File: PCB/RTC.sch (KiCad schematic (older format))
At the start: 5 parts, among them U8 DS3231M

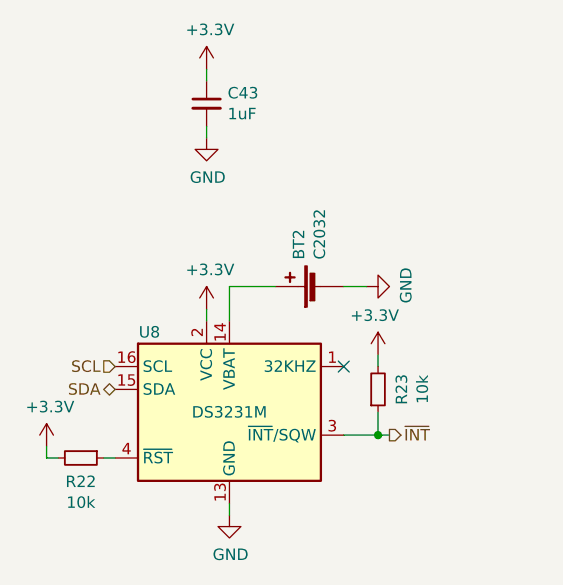
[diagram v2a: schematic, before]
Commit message: Increased VCC from 3v3 to 5v
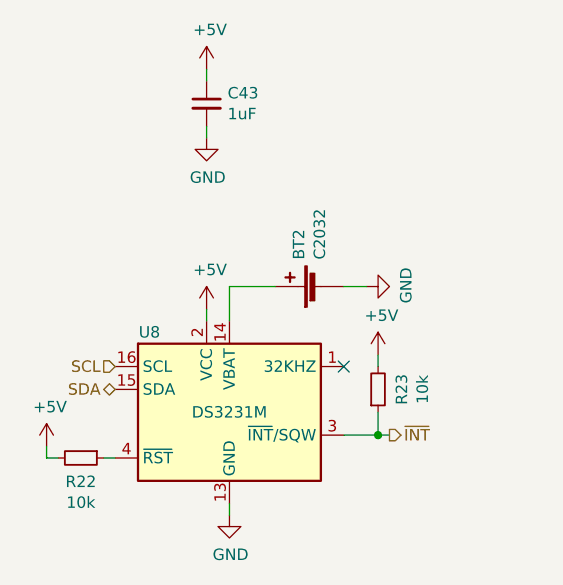
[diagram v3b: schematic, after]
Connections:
- net +3V3 renamed +5V
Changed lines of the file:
@@
 $Descr A4 11693 8268
 encoding utf-8
-Sheet 15 25
+Sheet 16 25
 Title ""
 Date ""
@@
 	0    -1   -1   0
 $EndComp
-$Comp
-L power:+3.3V #PWR0118
-U 1 1 5E875558
-P 5500 3650
-F 0 "#PWR0118" H 5500 3500 50  0001 C CNN
-F 1 "+3.3V" H 5515 3823 50  0000 C CNN
-F 2 "" H 5500 3650 50  0001 C CNN
-F 3 "" H 5500 3650 50  0001 C CNN
-	1    5500 3650
-	1    0    0    -1
-$EndComp
 Wire Wire Line
 	5500 3650 5500 3700
@@
 	1    0    0    -1
 $EndComp
-$Comp
-L power:+3.3V #PWR0116
-U 1 1 5E879CC5
-P 5500 2600
-F 0 "#PWR0116" H 5500 2450 50  0001 C CNN
-F 1 "+3.3V" H 5515 2773 50  0000 C CNN
-F 2 "" H 5500 2600 50  0001 C CNN
-F 3 "" H 5500 2600 50  0001 C CNN
-	1    5500 2600
-	1    0    0    -1
-$EndComp
 Wire Wire Line
 	5500 2600 5500 2650
@@
 	0    1    1    0
 $EndComp
-$Comp
-L power:+3.3V #PWR0115
-U 1 1 5E87C09D
-P 4800 4250
-F 0 "#PWR0115" H 4800 4100 50  0001 C CNN
-F 1 "+3.3V" H 4815 4423 50  0000 C CNN
-F 2 "" H 4800 4250 50  0001 C CNN
-F 3 "" H 4800 4250 50  0001 C CNN
-	1    4800 4250
-	1    0    0    -1
-$EndComp
 Wire Wire Line
 	4800 4250 4800 4300
@@
 	1    0    0    1
 $EndComp
-$Comp
-L power:+3.3V #PWR0121
-U 1 1 5E87E247
-P 6250 3850
-F 0 "#PWR0121" H 6250 3700 50  0001 C CNN
-F 1 "+3.3V" H 6265 4023 50  0000 C CNN
-F 2 "" H 6250 3850 50  0001 C CNN
-F 3 "" H 6250 3850 50  0001 C CNN
-	1    6250 3850
-	-1   0    0    -1
-$EndComp
 Wire Wire Line
 	6100 4200 6250 4200
@@
 	6300 4200 6250 4200
 Connection ~ 6250 4200
+$Comp
+L power:+5V #PWR?
+U 1 1 5E91AA2A
+P 4800 4250
+AR Path="/5E8A6686/5E91AA2A" Ref="#PWR?"  Part="1"
+AR Path="/5E87171F/5E91AA2A" Ref="#PWR?"  Part="1"
+F 0 "#PWR?" H 4800 4100 50  0001 C CNN
+F 1 "+5V" H 4815 4423 50  0000 C CNN
+F 2 "" H 4800 4250 50  0001 C CNN
+F 3 "" H 4800 4250 50  0001 C CNN
+	1    4800 4250
+	1    0    0    -1
+$EndComp
+$Comp
+L power:+5V #PWR?
+U 1 1 5E91AB6A
+P 5500 3650
+AR Path="/5E8A6686/5E91AB6A" Ref="#PWR?"  Part="1"
+AR Path="/5E87171F/5E91AB6A" Ref="#PWR?"  Part="1"
+F 0 "#PWR?" H 5500 3500 50  0001 C CNN
+F 1 "+5V" H 5515 3823 50  0000 C CNN
+F 2 "" H 5500 3650 50  0001 C CNN
+F 3 "" H 5500 3650 50  0001 C CNN
+	1    5500 3650
+	1    0    0    -1
+$EndComp
+$Comp
+L power:+5V #PWR?
+U 1 1 5E91B25B
+P 5500 2600
+F 0 "#PWR?" H 5500 2450 50  0001 C CNN
+F 1 "+5V" H 5515 2773 50  0000 C CNN
+F 2 "" H 5500 2600 50  0001 C CNN
+F 3 "" H 5500 2600 50  0001 C CNN
+	1    5500 2600
+	1    0    0    -1
+$EndComp
+$Comp
+L power:+5V #PWR?
+U 1 1 5E91BBAD
+P 6250 3850
+F 0 "#PWR?" H 6250 3700 50  0001 C CNN
+F 1 "+5V" H 6265 4023 50  0000 C CNN
+F 2 "" H 6250 3850 50  0001 C CNN
+F 3 "" H 6250 3850 50  0001 C CNN
+	1    6250 3850
+	1    0    0    -1
+$EndComp
 $EndSCHEMATC

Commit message: Added Humidity and temperature sensors
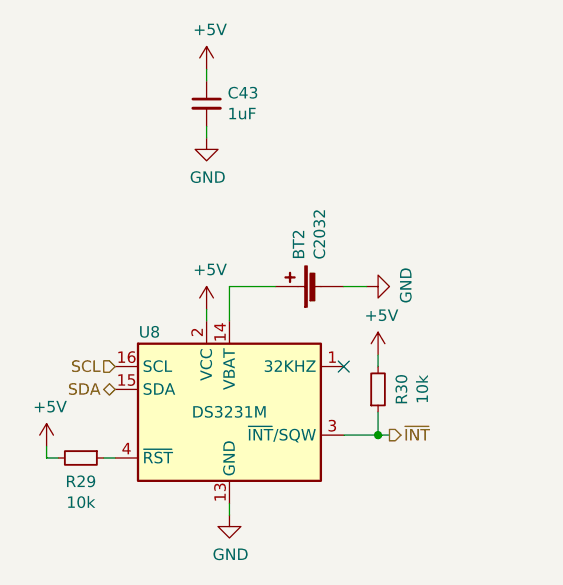
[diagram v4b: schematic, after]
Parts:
- renumbered R22 to R29, R23 to R30
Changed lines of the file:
@@
 $EndComp
 $Comp
-L power:GND #PWR0120
+L power:GND #PWR0123
 U 1 1 5E87532F
 P 6200 3550
-F 0 "#PWR0120" H 6200 3300 50  0001 C CNN
+F 0 "#PWR0123" H 6200 3300 50  0001 C CNN
 F 1 "GND" H 6205 3377 50  0000 C CNN
 F 2 "" H 6200 3550 50  0001 C CNN
@@
 NoConn ~ 6100 3900
 $Comp
-L power:GND #PWR0119
+L power:GND #PWR0122
 U 1 1 5E878241
 P 5600 4550
-F 0 "#PWR0119" H 5600 4300 50  0001 C CNN
+F 0 "#PWR0122" H 5600 4300 50  0001 C CNN
 F 1 "GND" H 5605 4377 50  0000 C CNN
 F 2 "" H 5600 4550 50  0001 C CNN
@@
 	5500 2600 5500 2650
 $Comp
-L power:GND #PWR0117
+L power:GND #PWR0120
 U 1 1 5E87A00D
 P 5500 2900
-F 0 "#PWR0117" H 5500 2650 50  0001 C CNN
+F 0 "#PWR0120" H 5500 2650 50  0001 C CNN
 F 1 "GND" H 5505 2727 50  0000 C CNN
 F 2 "" H 5500 2900 50  0001 C CNN
@@
 	5500 2850 5500 2900
 $Comp
-L Device:R_Small R22
+L Device:R_Small R29
 U 1 1 5E87BE49
 P 4950 4300
-F 0 "R22" V 5054 4300 50  0000 C CNN
+F 0 "R29" V 5054 4300 50  0000 C CNN
 F 1 "10k" V 5145 4300 50  0000 C CNN
 F 2 "" H 4950 4300 50  0001 C CNN
@@
 	5050 4300 5100 4300
 $Comp
-L Device:R_Small R23
+L Device:R_Small R30
 U 1 1 5E87E241
 P 6250 4000
-F 0 "R23" V 6354 4000 50  0000 C CNN
+F 0 "R30" V 6354 4000 50  0000 C CNN
 F 1 "10k" V 6445 4000 50  0000 C CNN
 F 2 "" H 6250 4000 50  0001 C CNN
@@
 P 4800 4250
 AR Path="/5E8A6686/5E91AA2A" Ref="#PWR?"  Part="1"
-AR Path="/5E87171F/5E91AA2A" Ref="#PWR?"  Part="1"
-F 0 "#PWR?" H 4800 4100 50  0001 C CNN
+AR Path="/5E87171F/5E91AA2A" Ref="#PWR0118"  Part="1"
+F 0 "#PWR0118" H 4800 4100 50  0001 C CNN
 F 1 "+5V" H 4815 4423 50  0000 C CNN
 F 2 "" H 4800 4250 50  0001 C CNN
@@
 P 5500 3650
 AR Path="/5E8A6686/5E91AB6A" Ref="#PWR?"  Part="1"
-AR Path="/5E87171F/5E91AB6A" Ref="#PWR?"  Part="1"
-F 0 "#PWR?" H 5500 3500 50  0001 C CNN
+AR Path="/5E87171F/5E91AB6A" Ref="#PWR0121"  Part="1"
+F 0 "#PWR0121" H 5500 3500 50  0001 C CNN
 F 1 "+5V" H 5515 3823 50  0000 C CNN
 F 2 "" H 5500 3650 50  0001 C CNN
@@
 U 1 1 5E91B25B
 P 5500 2600
-F 0 "#PWR?" H 5500 2450 50  0001 C CNN
+AR Path="/5E8A6686/5E91B25B" Ref="#PWR?"  Part="1"
+AR Path="/5E87171F/5E91B25B" Ref="#PWR0119"  Part="1"
+F 0 "#PWR0119" H 5500 2450 50  0001 C CNN
 F 1 "+5V" H 5515 2773 50  0000 C CNN
 F 2 "" H 5500 2600 50  0001 C CNN
@@
 U 1 1 5E91BBAD
 P 6250 3850
-F 0 "#PWR?" H 6250 3700 50  0001 C CNN
+AR Path="/5E8A6686/5E91BBAD" Ref="#PWR?"  Part="1"
+AR Path="/5E87171F/5E91BBAD" Ref="#PWR0124"  Part="1"
+F 0 "#PWR0124" H 6250 3700 50  0001 C CNN
 F 1 "+5V" H 6265 4023 50  0000 C CNN
 F 2 "" H 6250 3850 50  0001 C CNN

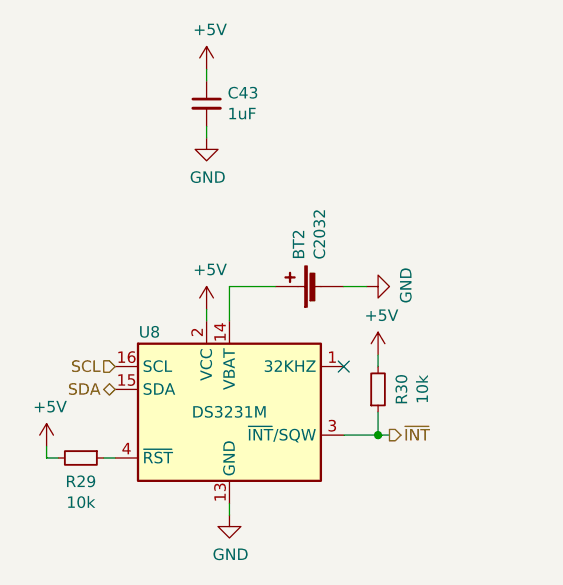
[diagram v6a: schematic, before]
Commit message: Added correct DRV breakout and added testpoints
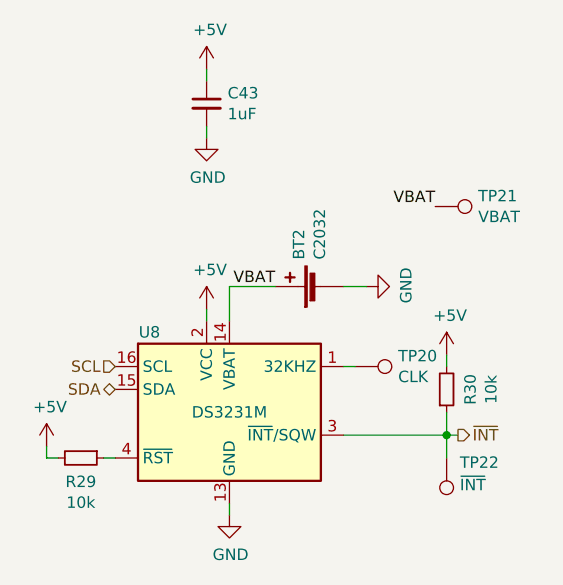
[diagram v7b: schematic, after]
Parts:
- added TP20: CLK, symbol Connector:TestPoint
- added TP21: VBAT, symbol Connector:TestPoint
- added TP22: ~INT, symbol Connector:TestPoint
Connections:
- net ~INT: now also TP22.1
- net at U8.1 (32KHZ): now also TP20.1
- net VBAT: now reaches BT2.1 (+), U8.14 (VBAT)
- net VBAT: now also TP21.1
- no-connect marks 1 -> 0
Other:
- moved on the sheet: R30
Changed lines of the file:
@@
 $EndComp
-Wire Wire Line
-	5500 3650 5500 3700
 Wire Wire Line
 	5800 3550 5600 3550
@@
 Wire Wire Line
 	6100 3550 6200 3550
-NoConn ~ 6100 3900
 $Comp
 L power:GND #PWR0122
@@
 L Device:R_Small R30
 U 1 1 5E87E241
-P 6250 4000
-F 0 "R30" V 6354 4000 50  0000 C CNN
-F 1 "10k" V 6445 4000 50  0000 C CNN
-F 2 "" H 6250 4000 50  0001 C CNN
-F 3 "" H 6250 4000 50  0001 C CNN
-	1    6250 4000
+P 6550 4000
+F 0 "R30" V 6654 4000 50  0000 C CNN
+F 1 "10k" V 6745 4000 50  0000 C CNN
+F 2 "" H 6550 4000 50  0001 C CNN
+F 3 "" H 6550 4000 50  0001 C CNN
+	1    6550 4000
 	1    0    0    1
 $EndComp
 Wire Wire Line
-	6100 4200 6250 4200
+	6100 4200 6550 4200
 Wire Wire Line
-	6250 4200 6250 4100
+	6550 4200 6550 4100
 Wire Wire Line
-	6250 3900 6250 3850
-Text HLabel 6300 4200 2    50   Output ~ 0
+	6550 3900 6550 3850
+Text HLabel 6600 4200 2    50   Output ~ 0
 ~INT
 Wire Wire Line
-	6300 4200 6250 4200
-Connection ~ 6250 4200
+	6600 4200 6550 4200
+Connection ~ 6550 4200
 $Comp
 L power:+5V #PWR?
@@
 F 3 "" H 4800 4250 50  0001 C CNN
 	1    4800 4250
-	1    0    0    -1
-$EndComp
-$Comp
-L power:+5V #PWR?
-U 1 1 5E91AB6A
-P 5500 3650
-AR Path="/5E8A6686/5E91AB6A" Ref="#PWR?"  Part="1"
-AR Path="/5E87171F/5E91AB6A" Ref="#PWR0121"  Part="1"
-F 0 "#PWR0121" H 5500 3500 50  0001 C CNN
-F 1 "+5V" H 5515 3823 50  0000 C CNN
-F 2 "" H 5500 3650 50  0001 C CNN
-F 3 "" H 5500 3650 50  0001 C CNN
-	1    5500 3650
 	1    0    0    -1
 $EndComp
@@
 L power:+5V #PWR?
 U 1 1 5E91BBAD
-P 6250 3850
+P 6550 3850
 AR Path="/5E8A6686/5E91BBAD" Ref="#PWR?"  Part="1"
 AR Path="/5E87171F/5E91BBAD" Ref="#PWR0124"  Part="1"
-F 0 "#PWR0124" H 6250 3700 50  0001 C CNN
-F 1 "+5V" H 6265 4023 50  0000 C CNN
-F 2 "" H 6250 3850 50  0001 C CNN
-F 3 "" H 6250 3850 50  0001 C CNN
-	1    6250 3850
+F 0 "#PWR0124" H 6550 3700 50  0001 C CNN
+F 1 "+5V" H 6565 4023 50  0000 C CNN
+F 2 "" H 6550 3850 50  0001 C CNN
+F 3 "" H 6550 3850 50  0001 C CNN
+	1    6550 3850
 	1    0    0    -1
 $EndComp
+$Comp
+L Connector:TestPoint TP?
+U 1 1 5E93A279
+P 6150 3900
+AR Path="/5E93A279" Ref="TP?"  Part="1"
+AR Path="/5E87171F/5E93A279" Ref="TP20"  Part="1"
+F 0 "TP20" V 6104 4088 50  0000 L CNN
+F 1 "CLK" V 6195 4088 50  0000 L CNN
+F 2 "" H 6350 3900 50  0001 C CNN
+F 3 "~" H 6350 3900 50  0001 C CNN
+	1    6150 3900
+	0    1    1    0
+$EndComp
+$Comp
+L Connector:TestPoint TP?
+U 1 1 5E93A65A
+P 6550 4300
+AR Path="/5E93A65A" Ref="TP?"  Part="1"
+AR Path="/5E87171F/5E93A65A" Ref="TP22"  Part="1"
+F 0 "TP22" H 6492 4320 50  0000 R CNN
+F 1 "~INT" H 6492 4418 50  0000 R CNN
+F 2 "" H 6750 4300 50  0001 C CNN
+F 3 "~" H 6750 4300 50  0001 C CNN
+	1    6550 4300
+	-1   0    0    1
+$EndComp
+Wire Wire Line
+	6150 3900 6100 3900
+Wire Wire Line
+	6550 4300 6550 4200
+$Comp
+L Connector:TestPoint TP?
+U 1 1 5E93C9CD
+P 6500 3200
+AR Path="/5E93C9CD" Ref="TP?"  Part="1"
+AR Path="/5E87171F/5E93C9CD" Ref="TP21"  Part="1"
+F 0 "TP21" V 6454 3388 50  0000 L CNN
+F 1 "VBAT" V 6545 3388 50  0000 L CNN
+F 2 "" H 6700 3200 50  0001 C CNN
+F 3 "~" H 6700 3200 50  0001 C CNN
+	1    6500 3200
+	0    1    1    0
+$EndComp
+Wire Wire Line
+	5500 3650 5500 3700
+$Comp
+L power:+5V #PWR?
+U 1 1 5E91AB6A
+P 5500 3650
+AR Path="/5E8A6686/5E91AB6A" Ref="#PWR?"  Part="1"
+AR Path="/5E87171F/5E91AB6A" Ref="#PWR0121"  Part="1"
+F 0 "#PWR0121" H 5500 3500 50  0001 C CNN
+F 1 "+5V" H 5515 3823 50  0000 C CNN
+F 2 "" H 5500 3650 50  0001 C CNN
+F 3 "" H 5500 3650 50  0001 C CNN
+	1    5500 3650
+	1    0    0    -1
+$EndComp
+Text Label 6500 3200 2    50   ~ 0
+VBAT
+Text Label 5800 3550 2    50   ~ 0
+VBAT
 $EndSCHEMATC

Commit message: Added remaining test points
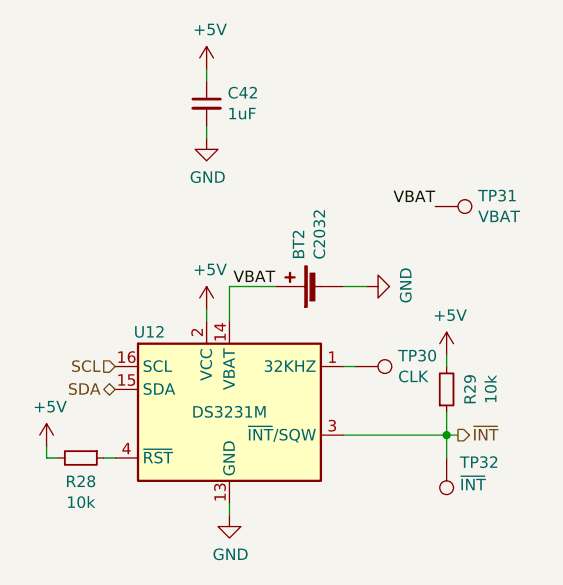
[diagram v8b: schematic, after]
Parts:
- renumbered C43 to C42, R29 to R28, R30 to R29, TP20 to TP30, TP21 to TP31, TP22 to TP32, U8 to U12
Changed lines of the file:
@@
 $EndDescr
 $Comp
-L Timer_RTC:DS3231M U8
+L Timer_RTC:DS3231M U12
 U 1 1 5E873E81
 P 5600 4100
-F 0 "U8" H 5250 4450 50  0000 C CNN
+F 0 "U12" H 5250 4450 50  0000 C CNN
 F 1 "DS3231M" H 5600 4100 50  0000 C CNN
 F 2 "Package_SO:SOIC-16W_7.5x10.3mm_P1.27mm" H 5600 3500 50  0001 C CNN
@@
 $EndComp
 $Comp
-L power:GND #PWR0123
+L power:GND #PWR0120
 U 1 1 5E87532F
 P 6200 3550
-F 0 "#PWR0123" H 6200 3300 50  0001 C CNN
+F 0 "#PWR0120" H 6200 3300 50  0001 C CNN
 F 1 "GND" H 6205 3377 50  0000 C CNN
 F 2 "" H 6200 3550 50  0001 C CNN
@@
 	6100 3550 6200 3550
 $Comp
-L power:GND #PWR0122
+L power:GND #PWR0119
 U 1 1 5E878241
 P 5600 4550
-F 0 "#PWR0122" H 5600 4300 50  0001 C CNN
+F 0 "#PWR0119" H 5600 4300 50  0001 C CNN
 F 1 "GND" H 5605 4377 50  0000 C CNN
 F 2 "" H 5600 4550 50  0001 C CNN
@@
 SCL
 $Comp
-L Device:C_Small C43
+L Device:C_Small C42
 U 1 1 5E879AEF
 P 5500 2750
-F 0 "C43" H 5592 2796 50  0000 L CNN
+F 0 "C42" H 5592 2796 50  0000 L CNN
 F 1 "1uF" H 5592 2705 50  0000 L CNN
 F 2 "" H 5500 2750 50  0001 C CNN
@@
 	5500 2600 5500 2650
 $Comp
-L power:GND #PWR0120
+L power:GND #PWR0117
 U 1 1 5E87A00D
 P 5500 2900
-F 0 "#PWR0120" H 5500 2650 50  0001 C CNN
+F 0 "#PWR0117" H 5500 2650 50  0001 C CNN
 F 1 "GND" H 5505 2727 50  0000 C CNN
 F 2 "" H 5500 2900 50  0001 C CNN
@@
 	5500 2850 5500 2900
 $Comp
-L Device:R_Small R29
+L Device:R_Small R28
 U 1 1 5E87BE49
 P 4950 4300
-F 0 "R29" V 5054 4300 50  0000 C CNN
+F 0 "R28" V 5054 4300 50  0000 C CNN
 F 1 "10k" V 5145 4300 50  0000 C CNN
 F 2 "" H 4950 4300 50  0001 C CNN
@@
 	5050 4300 5100 4300
 $Comp
-L Device:R_Small R30
+L Device:R_Small R29
 U 1 1 5E87E241
 P 6550 4000
-F 0 "R30" V 6654 4000 50  0000 C CNN
+F 0 "R29" V 6654 4000 50  0000 C CNN
 F 1 "10k" V 6745 4000 50  0000 C CNN
 F 2 "" H 6550 4000 50  0001 C CNN
@@
 P 4800 4250
 AR Path="/5E8A6686/5E91AA2A" Ref="#PWR?"  Part="1"
-AR Path="/5E87171F/5E91AA2A" Ref="#PWR0118"  Part="1"
-F 0 "#PWR0118" H 4800 4100 50  0001 C CNN
+AR Path="/5E87171F/5E91AA2A" Ref="#PWR0115"  Part="1"
+F 0 "#PWR0115" H 4800 4100 50  0001 C CNN
 F 1 "+5V" H 4815 4423 50  0000 C CNN
 F 2 "" H 4800 4250 50  0001 C CNN
@@
 P 5500 2600
 AR Path="/5E8A6686/5E91B25B" Ref="#PWR?"  Part="1"
-AR Path="/5E87171F/5E91B25B" Ref="#PWR0119"  Part="1"
-F 0 "#PWR0119" H 5500 2450 50  0001 C CNN
+AR Path="/5E87171F/5E91B25B" Ref="#PWR0116"  Part="1"
+F 0 "#PWR0116" H 5500 2450 50  0001 C CNN
 F 1 "+5V" H 5515 2773 50  0000 C CNN
 F 2 "" H 5500 2600 50  0001 C CNN
@@
 P 6550 3850
 AR Path="/5E8A6686/5E91BBAD" Ref="#PWR?"  Part="1"
-AR Path="/5E87171F/5E91BBAD" Ref="#PWR0124"  Part="1"
-F 0 "#PWR0124" H 6550 3700 50  0001 C CNN
+AR Path="/5E87171F/5E91BBAD" Ref="#PWR0121"  Part="1"
+F 0 "#PWR0121" H 6550 3700 50  0001 C CNN
 F 1 "+5V" H 6565 4023 50  0000 C CNN
 F 2 "" H 6550 3850 50  0001 C CNN
@@
 P 6150 3900
 AR Path="/5E93A279" Ref="TP?"  Part="1"
-AR Path="/5E87171F/5E93A279" Ref="TP20"  Part="1"
-F 0 "TP20" V 6104 4088 50  0000 L CNN
+AR Path="/5E87171F/5E93A279" Ref="TP30"  Part="1"
+F 0 "TP30" V 6104 4088 50  0000 L CNN
 F 1 "CLK" V 6195 4088 50  0000 L CNN
 F 2 "" H 6350 3900 50  0001 C CNN
@@
 P 6550 4300
 AR Path="/5E93A65A" Ref="TP?"  Part="1"
-AR Path="/5E87171F/5E93A65A" Ref="TP22"  Part="1"
-F 0 "TP22" H 6492 4320 50  0000 R CNN
+AR Path="/5E87171F/5E93A65A" Ref="TP32"  Part="1"
+F 0 "TP32" H 6492 4320 50  0000 R CNN
 F 1 "~INT" H 6492 4418 50  0000 R CNN
 F 2 "" H 6750 4300 50  0001 C CNN
@@
 P 6500 3200
 AR Path="/5E93C9CD" Ref="TP?"  Part="1"
-AR Path="/5E87171F/5E93C9CD" Ref="TP21"  Part="1"
-F 0 "TP21" V 6454 3388 50  0000 L CNN
+AR Path="/5E87171F/5E93C9CD" Ref="TP31"  Part="1"
+F 0 "TP31" V 6454 3388 50  0000 L CNN
 F 1 "VBAT" V 6545 3388 50  0000 L CNN
 F 2 "" H 6700 3200 50  0001 C CNN
@@
 P 5500 3650
 AR Path="/5E8A6686/5E91AB6A" Ref="#PWR?"  Part="1"
-AR Path="/5E87171F/5E91AB6A" Ref="#PWR0121"  Part="1"
-F 0 "#PWR0121" H 5500 3500 50  0001 C CNN
+AR Path="/5E87171F/5E91AB6A" Ref="#PWR0118"  Part="1"
+F 0 "#PWR0118" H 5500 3500 50  0001 C CNN
 F 1 "+5V" H 5515 3823 50  0000 C CNN
 F 2 "" H 5500 3650 50  0001 C CNN
